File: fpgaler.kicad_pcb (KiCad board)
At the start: 4 copper layers, 245.2 x 139.3 mm, 283 parts, among them J1 USB_C_Receptacle_USB2.0, J2 BATT, J3 JTAG, J4 FTDI_RST, Q1 BC817, SW1 RotaryEncoder_Switch, SW2 RotaryEncoder_Switch, SW3 K1, SW4 K2, SW5 PROGRAMN, SW6 K3, SW7 FPGA GSRN, SW8 K4, U1 TLV62569DRL, U10 XC6206PxxxMR, U2 TLV62569DRL, U3 NCP115-2.5, U4 BQ24232, U5 93LC56BT-I/OT, U6 FT2232HL, U7 CAT24C128, U8 LFE5U-25F-8MG285C, U9 W25Q128JVP, Y1 7M-12.000MAAJ

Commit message: Add sram and oscillator 27MHz
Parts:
- removed TP10, TP11, TP12, TP13, TP14, TP15, TP16, TP17, TP18, TP2, TP21, TP22, TP28, TP29, TP3, TP30, TP31, TP32, TP33, TP34, TP35, TP36, TP37, TP38, TP39, TP4, TP47, TP48, TP49, TP5, TP50, TP51, TP52, TP53, TP54, TP55, TP56, TP57, TP6, TP65, TP66, TP67, TP68, TP69, TP7, TP70, TP71, TP72, TP73, TP74, TP75, TP76, TP77, TP78, TP79, TP8, TP80, TP81, TP82, TP83, TP9: TestPoint, TestPoint:TestPoint_THTPad_D1.5mm_Drill0.7mm
- added C56: 100nF, Capacitor_SMD:C_0603_1608Metric, F.Cu at (144.1, 90.6)
- added C57: 100nF, Capacitor_SMD:C_0603_1608Metric, F.Cu at (227.8, 109.2)
- added C58: 100nF, Capacitor_SMD:C_0603_1608Metric, F.Cu at (211.3, 109.2)
- added J5: VGA, EasyEDA_Lib:DSUB-TH_HYC06-HDR15B-060, F.Cu at (216.1, 81.5)
- added J6: DB9 Expander, Connector_Dsub:DSUB-9_Pins_Horizontal_P2.77x2.84mm_EdgePinOffset4.94mm_Housed_MountingHolesOffset4.94mm, F.Cu at (184.5, 75.3)
- added R103: 100R, Resistor_SMD:R_0603_1608Metric, F.Cu at (204.8, 84.5)
- added R104: 100R, Resistor_SMD:R_0603_1608Metric, F.Cu at (204.9, 86.2)
- added R105: 3.9k, Resistor_SMD:R_0603_1608Metric, F.Cu at (209.2, 84.6)
- added R106: 2k, Resistor_SMD:R_0603_1608Metric, F.Cu at (209.2, 87.1)
- added R107: 1k, Resistor_SMD:R_0603_1608Metric, F.Cu at (209.2, 89.6)
- added R108: 3.9k, Resistor_SMD:R_0603_1608Metric, F.Cu at (209.3, 82.4)
- added R109: 2k, Resistor_SMD:R_0603_1608Metric, F.Cu at (209.4, 78.0)
- added R110: 1k, Resistor_SMD:R_0603_1608Metric, F.Cu at (209.4, 80.5)
- added R111: 3.9k, Resistor_SMD:R_0603_1608Metric, F.Cu at (209.2, 70.0)
- added R112: 2k, Resistor_SMD:R_0603_1608Metric, F.Cu at (209.2, 72.5)
- added R113: 1k, Resistor_SMD:R_0603_1608Metric, F.Cu at (209.2, 75.0)
- added R114: 22R, Resistor_SMD:R_0603_1608Metric, F.Cu at (146.6, 90.6)
- added R115: 22R, Resistor_SMD:R_0603_1608Metric, F.Cu at (149.2, 90.6)
- added R116: 22R, Resistor_SMD:R_0603_1608Metric, F.Cu at (151.7, 90.6)
- added R117: 22R, Resistor_SMD:R_0603_1608Metric, F.Cu at (154.2, 90.6)
- added R118: 22R, Resistor_SMD:R_0603_1608Metric, F.Cu at (144.1, 86.5)
- added R119: 22R, Resistor_SMD:R_0603_1608Metric, F.Cu at (146.6, 86.5)
- added R120: 22R, Resistor_SMD:R_0603_1608Metric, F.Cu at (149.2, 86.5)
- added R121: 22R, Resistor_SMD:R_0603_1608Metric, F.Cu at (151.7, 86.5)
- added R122: 22R, Resistor_SMD:R_0603_1608Metric, F.Cu at (154.2, 86.5)
- added R123: 22R, Resistor_SMD:R_0603_1608Metric, F.Cu at (144.1, 82.5)
- added R124: 22R, Resistor_SMD:R_0603_1608Metric, F.Cu at (146.6, 82.5)
- added R125: 22R, Resistor_SMD:R_0603_1608Metric, F.Cu at (149.2, 82.5)
- added U11: IS62WV51216BLL-55TLI, EasyEDA_Lib:TSOP-44_L18.4-W10.2-P0.80-LS11.8-BL, F.Cu at (219.3, 108.4)
- added X1: 27MHz, EasyEDA_Lib:OSC-SMD_4P-L3.2-W2.5-BL, F.Cu at (157.7, 89.7)
- moved L2 134.5 mm to (261.2, 158.3)
- moved C10 134.5 mm to (264.1, 140.6)
- moved C17 134.5 mm to (264.1, 149.7)
- moved C19 134.5 mm to (247.0, 150.8)
- moved R28 134.5 mm to (255.8, 140.4)
- moved R31 134.5 mm to (255.8, 147.9)
- moved R32 134.5 mm to (255.8, 150.4)
- moved R34 134.5 mm to (259.8, 140.4)
- moved U2 134.5 mm to (251.5, 155.9)
- moved C15 134.5 mm to (251.8, 142.9)
- moved R33 134.5 mm to (255.8, 152.9)
- moved C20 130.8 mm to (148.6, 172.1)
- moved J2 130.8 mm to (143.4, 172.9)
- moved R35 130.8 mm to (146.8, 161.9)
- moved R38 130.8 mm to (151.6, 161.9)
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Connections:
- R56 pad 2: /FTDI/TXD_UART -> /FPGA/TXD_UART
- R57 pad 2: /FTDI/RXD_UART -> /FPGA/RXD_UART
- R59 pad 2: /FTDI/SCL0 -> /FPGA/SCL0
- R60 pad 2: /FTDI/SDA0 -> /FPGA/SDA0
- R61 pad 2: /FTDI/SDA0 -> /FPGA/SDA0
- R67 pad 1: Net-(U8C-PR23A/PCLKT2_1) -> Net-(U8G-PB4A/D7/IO7)
- R68 pad 1: Net-(U8C-PR23B/PCLKC2_1) -> Net-(U8G-PB4B/D6/IO6)
- R69 pad 1: Net-(U8C-PR23C/PCLKT2_0) -> Net-(U8G-PB6A/D5/MISO2/IO5)
- R70 pad 1: Net-(U8C-PR23D/PCLKC2_0) -> Net-(U8G-PB6B/D4/MOSI2/IO4)
- R73 pad 1: Net-(U8D-PR32A) -> Net-(U8D-PR35A)
- R74 pad 1: Net-(U8D-PR32B) -> Net-(U8D-PR35B/VREF1_3)
- R75 pad 1: Net-(U8D-PR35A) -> Net-(U8D-PR35C)
- R76 pad 1: Net-(U8D-PR35B/VREF1_3) -> Net-(U8D-PR35D)
- R77 pad 1: Net-(U8D-PR35C) -> Net-(U8D-PR38A)
- R78 pad 1: Net-(U8D-PR35D) -> Net-(U8D-PR38B)
- R79 pad 1: Net-(U8D-PR38A) -> Net-(U8D-PR38C)
- R80 pad 1: Net-(U8D-PR38B) -> Net-(U8D-PR38D)
- R81 pad 1: Net-(U8D-PR38C) -> Net-(U8D-PR41A)
- R82 pad 1: Net-(U8D-PR38D) -> Net-(U8D-PR41B)
- R83 pad 1: Net-(U8D-PR41A) -> Net-(U8D-PR41C)
- R84 pad 1: Net-(U8D-PR41B) -> Net-(U8D-PR41D)
- R85 pad 1: Net-(U8D-PR41C) -> Net-(U8D-PR44A)
- R86 pad 1: Net-(U8D-PR41D) -> Net-(U8D-PR44B)
- R87 pad 1: Net-(U8D-PR44A) -> Net-(U8D-PR44C)
- R88 pad 1: Net-(U8D-PR44B) -> Net-(U8D-PR44D)
- R89 pad 1: Net-(U8D-PR44C) -> Net-(U8D-PR47C/LRC_GPLL0T_IN)
- R90 pad 1: Net-(U8D-PR44D) -> Net-(U8D-PR47D/LRC_GPLL0C_IN)
- U8 pad A15: Net-(U8F-PL14D) -> /FPGA/VGA_R1
- U8 pad A16: Net-(U8F-PL20B) -> /FPGA/VGA_G2
- U8 pad A17: Net-(U8F-PL23A/PCLKT7_1) -> /FPGA/VGA_B1
- U8 pad A2: Net-(U8C-PR20C/GR_PCLK2_0) -> /FPGA/~{WE}
- U8 pad A3: Net-(U8C-PR20A/GR_PCLK2_1) -> /FPGA/IO14
- U8 pad A4: Net-(U8C-PR11B) -> /FPGA/IO07
- U8 pad A6: Net-(U8C-PR11A) -> /FPGA/IO06
- U8 pad A7: Net-(U8C-PR8B) -> /FPGA/IO05
- U8 pad A9: /FPGA/REF_CLK -> Net-(U8B-PT35A/PCLKT1_0)
- U8 pad B1: Net-(U8C-PR23B/PCLKC2_1) -> /FPGA/~{OE}
- U8 pad B15: Net-(U8F-PL20A/GR_PCLK7_1) -> /FPGA/VGA_G1
- U8 pad B17: Net-(U8F-PL23B/PCLKC7_1) -> /FPGA/VGA_B2
- U8 pad B18: Net-(U8F-PL23C/PCLKT7_0) -> /FPGA/VGA_HSYNC
- U8 pad B2: Net-(U8C-PR20B) -> /FPGA/IO15
- U8 pad B4: Net-(U8C-PR14C/VREF1_2) -> /FPGA/IO10
- U8 pad B6: Net-(U8C-PR8A) -> /FPGA/IO04
- U8 pad B7: Net-(U8C-PR2B/S0_IN) -> /FPGA/IO01
- U8 pad C1: Net-(U8C-PR23C/PCLKT2_0) -> /FPGA/~{UB}
- U8 pad C15: Net-(U8F-PL14C/VREF1_7) -> /FPGA/VGA_R0
- U8 pad C16: Net-(U8F-PL20C/GR_PCLK7_0) -> /FPGA/VGA_B0
- U8 pad C17: Net-(U8F-PL23D/PCLKC7_0) -> /FPGA/VGA_VSYNC
- U8 pad C2: Net-(U8C-PR17B) -> /FPGA/IO13
- U8 pad C3: Net-(U8C-PR14D) -> /FPGA/IO11
- U8 pad C4: Net-(U8C-PR14B) -> /FPGA/IO09
- U8 pad C6: Net-(U8C-PR5B) -> /FPGA/IO03
- U8 pad C7: Net-(U8C-PR2A) -> /FPGA/IO00
- U8 pad D1: Net-(U8C-PR23D/PCLKC2_0) -> /FPGA/~{LB}
- U8 pad D15: Net-(U8F-PL17A) -> /FPGA/VGA_R2
- U8 pad D16: Net-(U8F-PL17B) -> /FPGA/VGA_G0
- U8 pad D2: Net-(U8C-PR23A/PCLKT2_1) -> /FPGA/~{CS1}
- U8 pad D3: Net-(U8C-PR17A) -> /FPGA/IO12
- U8 pad D4: Net-(U8C-PR14A) -> /FPGA/IO08
- U8 pad D6: Net-(U8C-PR5A) -> /FPGA/IO02
- U8 pad G1: Net-(U8D-PR32B) -> unconnected-(U8D-PR32B-PadG1)
- U8 pad G15: Net-(U8E-PL35A) -> /FPGA/A3
- U8 pad G16: Net-(U8E-PL29D) -> /FPGA/A0
- U8 pad G18: Net-(U8E-PL32A) -> /FPGA/A1
- U8 pad H15: Net-(U8E-PL35B/VREF1_6) -> /FPGA/A4
- U8 pad H16: Net-(U8E-PL35C) -> /FPGA/A5
- U8 pad H17: Net-(U8E-PL32B) -> /FPGA/A2
- U8 pad H18: Net-(U8E-PL38D) -> /FPGA/A8
- U8 pad J16: Net-(U8E-PL35D) -> /FPGA/A6
- U8 pad J17: Net-(U8E-PL38C) -> /FPGA/A7
- U8 pad J18: Net-(U8E-PL41A) -> /FPGA/A9
- U8 pad K15: Net-(U8E-PL41D) -> /FPGA/A12
- U8 pad K16: Net-(U8E-PL41C) -> /FPGA/A11
- U8 pad K17: Net-(U8E-PL44A) -> /FPGA/A13
- U8 pad K18: Net-(U8E-PL41B) -> /FPGA/A10
- U8 pad L15: Net-(U8E-PL44C) -> /FPGA/A15
- U8 pad L16: Net-(U8E-PL44D) -> /FPGA/A16
- U8 pad L18: Net-(U8E-PL44B) -> /FPGA/A14
- U8 pad M1: unconnected-(U8D-PR47C/LRC_GPLL0T_IN-PadM1) -> Net-(U8D-PR47C/LRC_GPLL0T_IN)
- U8 pad M16: Net-(U8E-PL47C/LLC_GPLL0T_IN) -> /FPGA/A17
- U8 pad M17: Net-(U8E-PL47D/LLC_GPLL0C_IN) -> /FPGA/A18
- U8 pad N1: unconnected-(U8D-PR47D/LRC_GPLL0C_IN-PadN1) -> Net-(U8D-PR47D/LRC_GPLL0C_IN)
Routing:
- net Net-(U8E-PL26B/PCLKC6_1): track 0.00 -> 26.9 mm
- net /FPGA/VGA_HSYNC: track 0.00 -> 24.3 mm
- net Net-(U8E-PL38D): track 22.2 -> 0.00 mm
- net /FPGA/VGA_VSYNC: track 0.00 -> 22.0 mm
- net /FPGA/VGA_B0: track 0.00 -> 22.0 mm, vias 0 -> 1
- net /FPGA/VGA_R0: track 0.00 -> 21.5 mm, vias 0 -> 1
- net /FPGA/VGA_B2: track 0.00 -> 21.2 mm
- net Net-(U8E-PL26C/PCLKT6_0): track 0.00 -> 20.1 mm
- net Net-(U8E-PL29D): track 19.8 -> 0.00 mm, vias 1 -> 0
- net Net-(U8E-PL41B): track 19.7 -> 0.00 mm
- net Net-(U8E-PL32A): track 19.4 -> 0.00 mm
- net Net-(U8E-PL35A): track 18.8 -> 0.00 mm, vias 1 -> 0
- net Net-(U8E-PL32B): track 18.4 -> 0.00 mm
- net Net-(U8E-PL35C): track 17.4 -> 0.00 mm, vias 1 -> 0
- net /FPGA/VGA_R2: track 0.00 -> 17.3 mm, vias 0 -> 1
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
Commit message: Routing sram
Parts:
- moved C13 35.0 mm to (224.8, 194.2)
- moved R29 35.0 mm to (231.0, 173.9)
- moved U10 35.0 mm to (231.6, 191.2)
- moved C11 35.0 mm to (234.5, 194.0)
- moved C14 35.0 mm to (239.3, 177.7)
- moved C16 35.0 mm to (227.0, 176.4)
- moved C18 35.0 mm to (222.2, 178.5)
- moved C9 35.0 mm to (227.0, 171.4)
- moved L1 35.0 mm to (236.4, 186.6)
- moved R27 35.0 mm to (227.0, 184.0)
- moved R30 35.0 mm to (231.0, 176.4)
- moved U1 35.0 mm to (228.5, 179.9)
- moved U3 35.0 mm to (230.9, 194.6)
- moved C1 23.8 mm to (194.7, 179.2)
- moved C2 23.8 mm to (195.0, 181.4)
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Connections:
- TP58 pad 1: Net-(U8E-PL26A/PCLKT6_1) -> unconnected-(TP58-Pad1)
- TP59 pad 1: Net-(U8E-PL26B/PCLKC6_1) -> unconnected-(TP59-Pad1)
- TP60 pad 1: Net-(U8E-PL26C/PCLKT6_0) -> unconnected-(TP60-Pad1)
- TP61 pad 1: Net-(U8E-PL26D/PCLKC6_0) -> unconnected-(TP61-Pad1)
- TP62 pad 1: Net-(U8E-PL29A/GR_PCLK6_0) -> unconnected-(TP62-Pad1)
- TP63 pad 1: Net-(U8E-PL29B) -> unconnected-(TP63-Pad1)
- TP64 pad 1: Net-(U8E-PL29C/GR_PCLK6_1) -> unconnected-(TP64-Pad1)
- U8 pad A15: /FPGA/VGA_R1 -> unconnected-(U8F-PL14D-PadA15)
- U8 pad A16: /FPGA/VGA_G2 -> unconnected-(U8F-PL20B-PadA16)
- U8 pad A17: /FPGA/VGA_B1 -> /FPGA/A4
- U8 pad A3: /FPGA/IO14 -> unconnected-(U8C-PR20A/GR_PCLK2_1-PadA3)
- U8 pad B1: /FPGA/~{OE} -> unconnected-(U8C-PR23B/PCLKC2_1-PadB1)
- U8 pad B15: /FPGA/VGA_G1 -> /FPGA/A7
- U8 pad B17: /FPGA/VGA_B2 -> /FPGA/A6
- U8 pad B18: /FPGA/VGA_HSYNC -> unconnected-(U8F-PL23C/PCLKT7_0-PadB18)
- U8 pad C1: /FPGA/~{UB} -> unconnected-(U8C-PR23C/PCLKT2_0-PadC1)
- U8 pad C15: /FPGA/VGA_R0 -> /FPGA/~{OE}
- U8 pad C16: /FPGA/VGA_B0 -> /FPGA/~{UB}
- U8 pad C17: /FPGA/VGA_VSYNC -> unconnected-(U8F-PL23D/PCLKC7_0-PadC17)
- U8 pad C18: Net-(U8E-PL26B/PCLKC6_1) -> unconnected-(U8E-PL26B/PCLKC6_1-PadC18)
- U8 pad C2: /FPGA/IO13 -> unconnected-(U8C-PR17B-PadC2)
- U8 pad D1: /FPGA/~{LB} -> unconnected-(U8C-PR23D/PCLKC2_0-PadD1)
- U8 pad D15: /FPGA/VGA_R2 -> /FPGA/~{LB}
- U8 pad D16: /FPGA/VGA_G0 -> unconnected-(U8F-PL17B-PadD16)
- U8 pad D17: Net-(U8E-PL26A/PCLKT6_1) -> unconnected-(U8E-PL26A/PCLKT6_1-PadD17)
- U8 pad D18: Net-(U8E-PL26C/PCLKT6_0) -> unconnected-(U8E-PL26C/PCLKT6_0-PadD18)
- U8 pad F15: Net-(U8E-PL29C/GR_PCLK6_1) -> /FPGA/IO14
- U8 pad F16: Net-(U8E-PL29B) -> unconnected-(U8E-PL29B-PadF16)
- U8 pad F17: Net-(U8E-PL29A/GR_PCLK6_0) -> unconnected-(U8E-PL29A/GR_PCLK6_0-PadF17)
- U8 pad F18: Net-(U8E-PL26D/PCLKC6_0) -> /FPGA/A2
- U8 pad G15: /FPGA/A3 -> /FPGA/IO13
- U8 pad H15: /FPGA/A4 -> unconnected-(U8E-PL35B/VREF1_6-PadH15)
- U8 pad H17: /FPGA/A2 -> unconnected-(U8E-PL32B-PadH17)
- U8 pad J16: /FPGA/A6 -> unconnected-(U8E-PL35D-PadJ16)
- U8 pad J17: /FPGA/A7 -> unconnected-(U8E-PL38C-PadJ17)
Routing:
- net Net-(U8G-PB4A/D7/IO7): track 0.28 -> 28.5 mm, vias 1 -> 2
- net unconnected-(U8F-PL23C/PCLKT7_0-PadB18): track 0.00 -> 27.6 mm
- net unconnected-(U8F-PL23D/PCLKC7_0-PadC17): track 0.00 -> 27.0 mm
- net Net-(U8E-PL26B/PCLKC6_1): track 26.9 -> 0.00 mm
- net Net-(U8G-PB4B/D6/IO6): track 0.28 -> 27.1 mm, vias 1 -> 2
- net /FPGA/A17: track 0.28 -> 26.4 mm, vias 1 -> 2
- net /FPGA/A15: track 0.28 -> 25.5 mm
- net unconnected-(U8E-PL26B/PCLKC6_1-PadC18): track 0.00 -> 25.0 mm
- net unconnected-(U8E-PL26A/PCLKT6_1-PadD17): track 0.00 -> 24.8 mm
- net /FPGA/VGA_HSYNC: track 24.3 -> 0.00 mm
- net unconnected-(U8E-PL29B-PadF16): track 0.00 -> 23.2 mm
- net unconnected-(U8E-PL26C/PCLKT6_0-PadD18): track 0.00 -> 23.0 mm
- net /FPGA/A12: track 0.28 -> 22.7 mm, vias 1 -> 2
- net /FPGA/VGA_VSYNC: track 22.0 -> 0.00 mm
- net /FPGA/VGA_B0: track 22.0 -> 0.00 mm, vias 1 -> 0
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
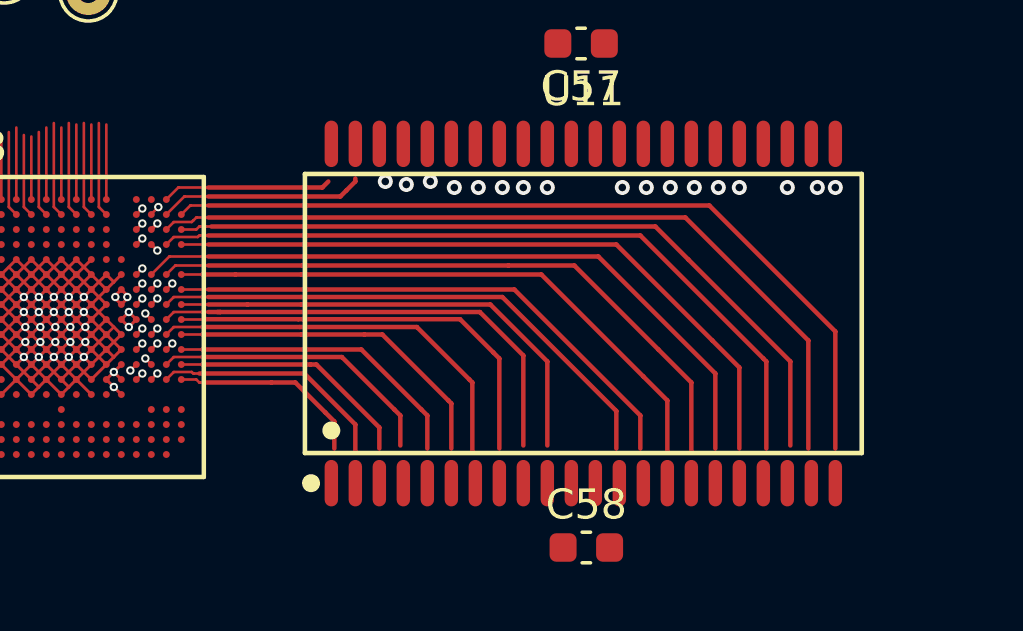
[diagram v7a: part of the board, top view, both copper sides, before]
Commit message: routing sram
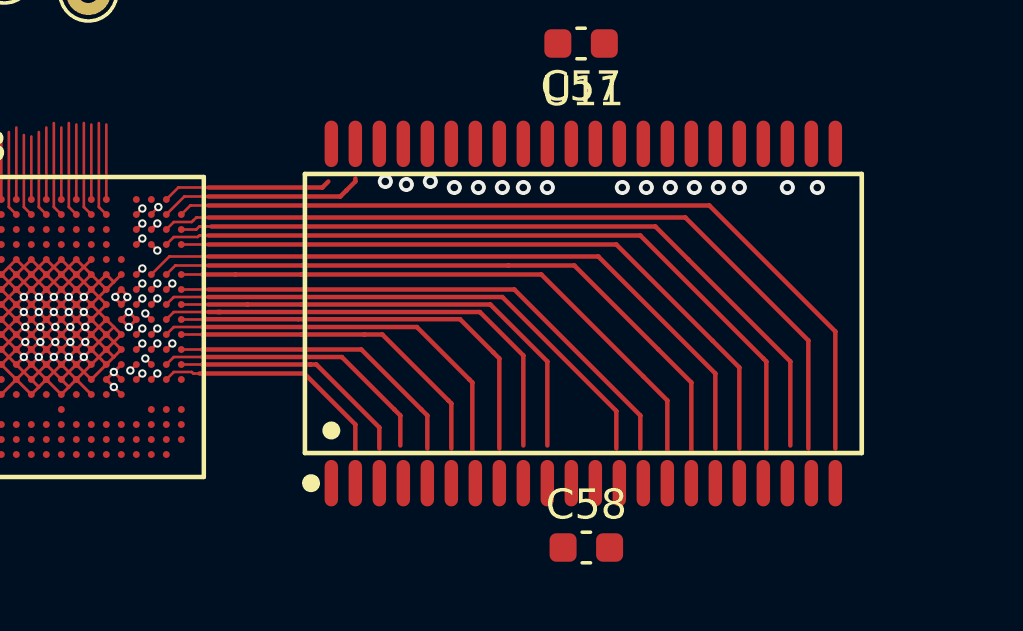
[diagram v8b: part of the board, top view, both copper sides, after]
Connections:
- R67 pad 1: Net-(U8G-PB4A/D7/IO7) -> unconnected-(R67-Pad1)
- R68 pad 1: Net-(U8G-PB4B/D6/IO6) -> unconnected-(R68-Pad1)
- R69 pad 1: Net-(U8G-PB6A/D5/MISO2/IO5) -> unconnected-(R69-Pad1)
- R70 pad 1: Net-(U8G-PB6B/D4/MOSI2/IO4) -> unconnected-(R70-Pad1)
- U8 pad A17: /FPGA/A4 -> /FPGA/A5
- U8 pad A2: /FPGA/~{WE} -> unconnected-(U8C-PR20C/GR_PCLK2_0-PadA2)
- U8 pad A4: /FPGA/IO07 -> unconnected-(U8C-PR11B-PadA4)
- U8 pad A6: /FPGA/IO06 -> unconnected-(U8C-PR11A-PadA6)
- U8 pad A7: /FPGA/IO05 -> unconnected-(U8C-PR8B-PadA7)
- U8 pad B18: unconnected-(U8F-PL23C/PCLKT7_0-PadB18) -> /FPGA/A12
- U8 pad B2: /FPGA/IO15 -> unconnected-(U8C-PR20B-PadB2)
- U8 pad B4: /FPGA/IO10 -> unconnected-(U8C-PR14C/VREF1_2-PadB4)
- U8 pad B6: /FPGA/IO04 -> unconnected-(U8C-PR8A-PadB6)
- U8 pad B7: /FPGA/IO01 -> unconnected-(U8C-PR2B/S0_IN-PadB7)
- U8 pad C17: unconnected-(U8F-PL23D/PCLKC7_0-PadC17) -> /FPGA/A13
- U8 pad C18: unconnected-(U8E-PL26B/PCLKC6_1-PadC18) -> /FPGA/A14
- U8 pad C3: /FPGA/IO11 -> unconnected-(U8C-PR14D-PadC3)
- U8 pad C4: /FPGA/IO09 -> unconnected-(U8C-PR14B-PadC4)
- U8 pad C6: /FPGA/IO03 -> unconnected-(U8C-PR5B-PadC6)
- U8 pad C7: /FPGA/IO00 -> unconnected-(U8C-PR2A-PadC7)
- U8 pad D16: unconnected-(U8F-PL17B-PadD16) -> /FPGA/IO15
- U8 pad D17: unconnected-(U8E-PL26A/PCLKT6_1-PadD17) -> /FPGA/A15
- U8 pad D18: unconnected-(U8E-PL26C/PCLKT6_0-PadD18) -> /FPGA/A16
- U8 pad D2: /FPGA/~{CS1} -> unconnected-(U8C-PR23A/PCLKT2_1-PadD2)
- U8 pad D3: /FPGA/IO12 -> unconnected-(U8C-PR17A-PadD3)
- U8 pad D4: /FPGA/IO08 -> unconnected-(U8C-PR14A-PadD4)
- U8 pad D6: /FPGA/IO02 -> unconnected-(U8C-PR5A-PadD6)
- U8 pad F16: unconnected-(U8E-PL29B-PadF16) -> /FPGA/~{WE}
- U8 pad F17: unconnected-(U8E-PL29A/GR_PCLK6_0-PadF17) -> /FPGA/IO07
- U8 pad F18: /FPGA/A2 -> /FPGA/IO06
- U8 pad G16: /FPGA/A0 -> /FPGA/IO12
- U8 pad G18: /FPGA/A1 -> /FPGA/IO05
- U8 pad H15: unconnected-(U8E-PL35B/VREF1_6-PadH15) -> /FPGA/IO10
- U8 pad H16: /FPGA/A5 -> /FPGA/IO11
- U8 pad H17: unconnected-(U8E-PL32B-PadH17) -> /FPGA/IO04
- U8 pad H18: /FPGA/A8 -> /FPGA/IO03
- U8 pad J16: unconnected-(U8E-PL35D-PadJ16) -> /FPGA/IO09
- U8 pad J17: unconnected-(U8E-PL38C-PadJ17) -> /FPGA/IO02
- U8 pad J18: /FPGA/A9 -> /FPGA/IO01
- U8 pad K15: /FPGA/A12 -> /FPGA/IO08
- U8 pad K16: /FPGA/A11 -> /FPGA/A18
- U8 pad K17: /FPGA/A13 -> /FPGA/IO00
- U8 pad K18: /FPGA/A10 -> /FPGA/~{CS1}
- U8 pad L15: /FPGA/A15 -> /FPGA/A9
- U8 pad L16: /FPGA/A16 -> /FPGA/A8
- U8 pad L18: /FPGA/A14 -> /FPGA/A0
- U8 pad M16: /FPGA/A17 -> /FPGA/A10
- U8 pad M17: /FPGA/A18 -> /FPGA/A1
- U8 pad M18: Net-(U8G-PB6B/D4/MOSI2/IO4) -> /FPGA/A2
- U8 pad N15: Net-(U8G-PB4A/D7/IO7) -> /FPGA/A4
- U8 pad N16: Net-(U8G-PB4B/D6/IO6) -> /FPGA/A11
- U8 pad N17: Net-(U8G-PB6A/D5/MISO2/IO5) -> /FPGA/A3
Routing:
- net Net-(U8G-PB4A/D7/IO7): track 28.5 -> 0.00 mm, vias 2 -> 0
- net unconnected-(U8F-PL23C/PCLKT7_0-PadB18): track 27.6 -> 0.00 mm
- net Net-(U8G-PB4B/D6/IO6): track 27.1 -> 0.00 mm, vias 2 -> 0
- net unconnected-(U8F-PL23D/PCLKC7_0-PadC17): track 27.0 -> 0.00 mm
- net /FPGA/A17: track 26.4 -> 0.00 mm, vias 2 -> 0
- net unconnected-(U8E-PL26B/PCLKC6_1-PadC18): track 25.0 -> 0.00 mm
- net unconnected-(U8E-PL26A/PCLKT6_1-PadD17): track 24.8 -> 0.00 mm
- net unconnected-(U8E-PL29B-PadF16): track 23.2 -> 0.00 mm
- net unconnected-(U8E-PL26C/PCLKT6_0-PadD18): track 23.0 -> 0.00 mm
- net /FPGA/IO08: track 0.00 -> 22.7 mm, vias 0 -> 2
- net /FPGA/~{WE}: track 1.50 -> 23.2 mm
- net unconnected-(U8E-PL29A/GR_PCLK6_0-PadF17): track 21.5 -> 0.00 mm
- net unconnected-(U8E-PL35D-PadJ16): track 21.4 -> 0.00 mm, vias 2 -> 0
- net /FPGA/IO09: track 0.00 -> 21.4 mm, vias 0 -> 2
- net unconnected-(U8E-PL35B/VREF1_6-PadH15): track 20.6 -> 0.00 mm, vias 2 -> 0
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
